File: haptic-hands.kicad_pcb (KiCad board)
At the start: 2 copper layers, 28.6 x 89 mm, 17 parts, among them M1 Motor_DC, SW1 SW_Push_45deg

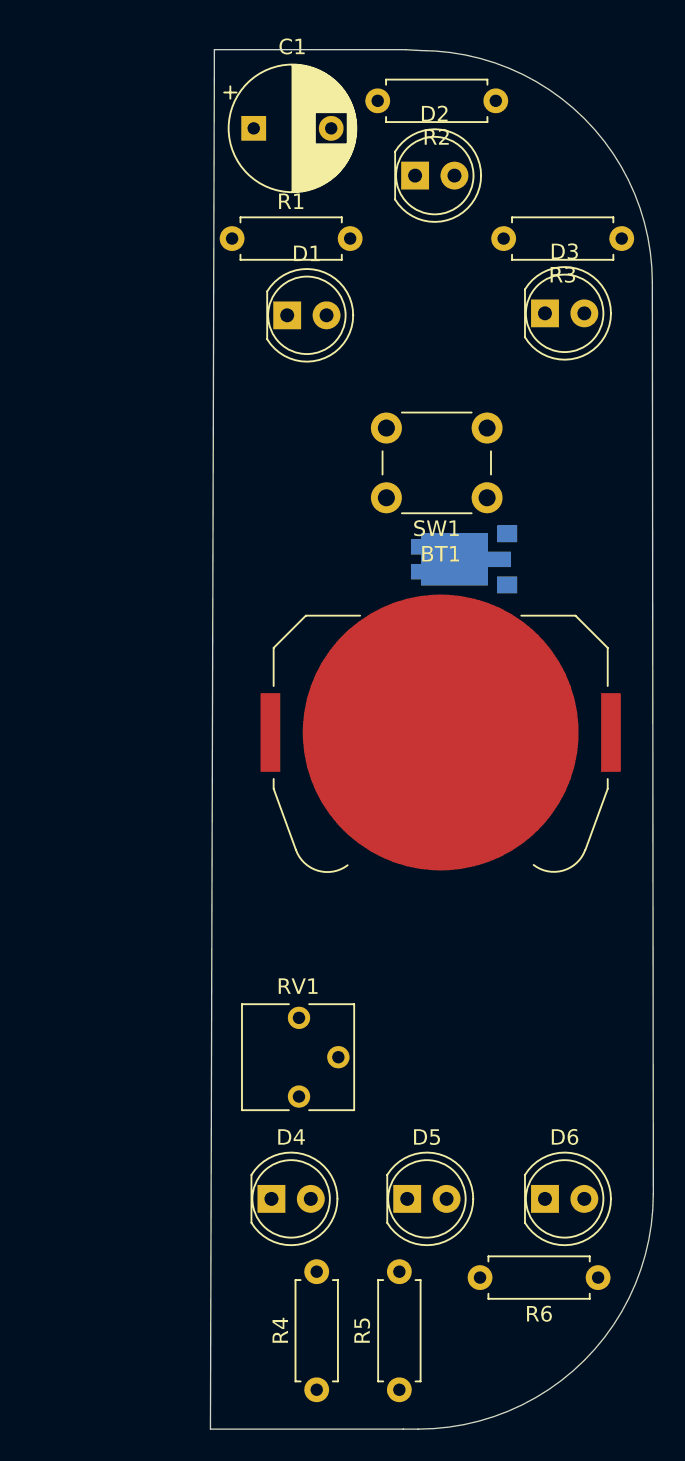
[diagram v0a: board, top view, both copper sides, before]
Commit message: Rearrange components, create board outline, route
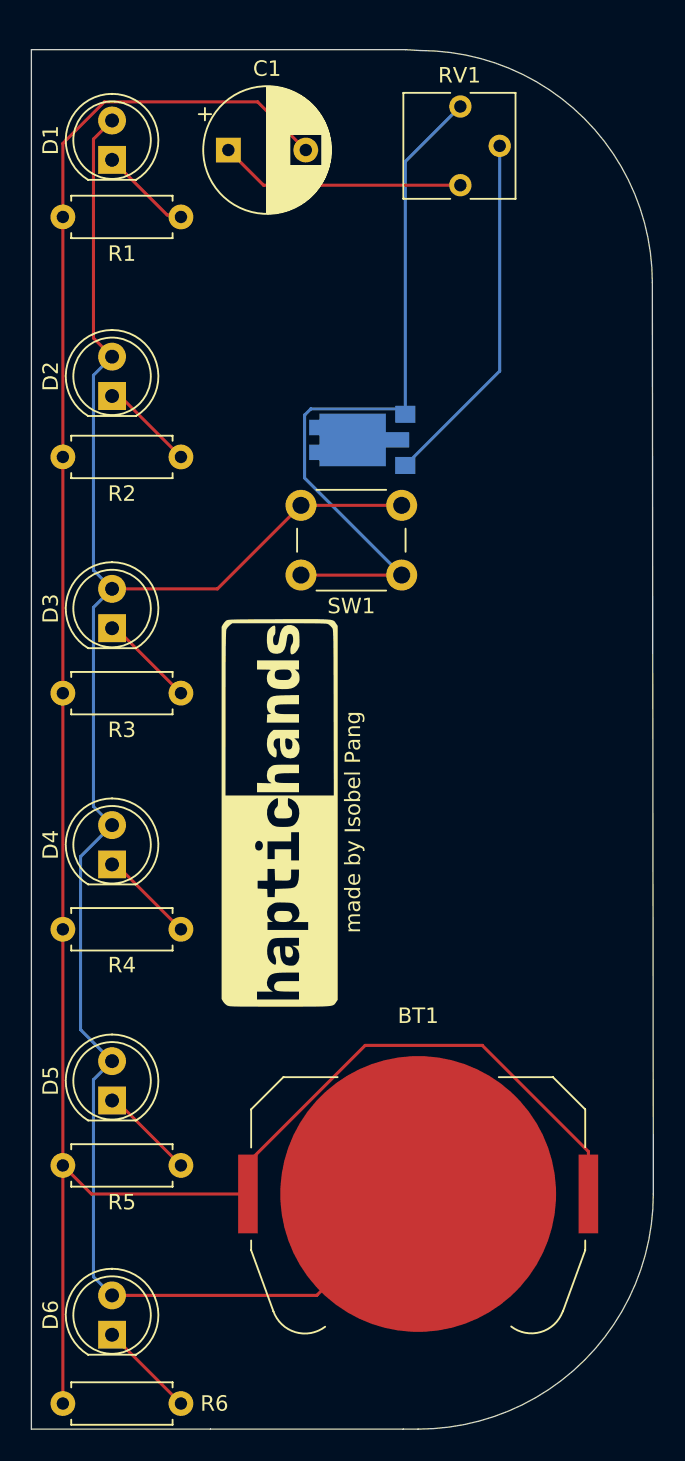
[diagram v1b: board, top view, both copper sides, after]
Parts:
- added G***: LOGO, LOGO, F.Cu at (129.5, 93.9)
- moved RV1 59.7 mm to (141.2, 53.3)
- moved R3 40.9 mm to (123.2, 86.1)
- moved D3 34.5 mm to (118.7, 81.9), turned to 90 degrees
- moved R4 31.0 mm to (123.2, 101.3), turned to 180 degrees
- moved R2 30.7 mm to (123.2, 70.9)
- moved BT1 29.8 mm to (138.5, 118.4)
- moved D6 29.3 mm to (118.7, 127.5), turned to 90 degrees
- moved R6 28.1 mm to (123.2, 132.0)
- moved D2 24.2 mm to (118.7, 66.9), turned to 90 degrees
- moved D4 23.9 mm to (118.7, 97.2), turned to 90 degrees
- moved R5 20.2 mm to (123.2, 116.6), turned to 180 degrees
- moved D5 20.1 mm to (118.7, 112.4), turned to 90 degrees
- moved D1 15.1 mm to (118.7, 51.7), turned to 90 degrees
- moved M1 10.1 mm to (133.3, 69.8)
- moved SW1 7.44 mm to (137.4, 78.5)
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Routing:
- net Net-(BT1-+): track 0.00 -> 144.8 mm
- net Net-(BT1--): track 0.00 -> 124.9 mm
- net Net-(M1--): track 0.00 -> 47.6 mm
- net Net-(M1-+): track 0.00 -> 23.2 mm
- net Net-(C1-Pad1): track 0.00 -> 15.9 mm
- net Net-(D6-K): track 0.00 -> 6.28 mm
- net Net-(D5-K): track 0.00 -> 6.18 mm
- net Net-(D3-K): track 0.00 -> 6.18 mm
- net Net-(D4-K): track 0.00 -> 6.18 mm
- net Net-(D2-K): track 0.00 -> 6.07 mm
- net Net-(D1-K): track 0.00 -> 5.97 mm
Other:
- board size 28.6 x 89 mm -> 40.1 x 89 mm
- board text added: "made by Isobel Pang"

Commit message: Route PCB
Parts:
- added G***: LOGO, LOGO, F.Cu at (138.4, 61.0)
- added G***: LOGO, LOGO, F.Cu at (137.4, 80.6)
- added G***: LOGO, LOGO, F.Cu at (146.8, 107.4)
- added G***: LOGO, LOGO, F.Cu at (148.0, 77.0)
- added G***: LOGO, LOGO, F.Cu at (119.5, 91.9)
- added G***: LOGO, LOGO, F.Cu at (137.5, 67.6)
- added G***: LOGO, LOGO, F.Cu at (138.2, 95.6)
- added G***: LOGO, LOGO, F.Cu at (125.6, 76.1)
- moved G*** 0.89 mm to (128.7, 93.9)

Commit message: Rework schematic
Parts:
- removed G*** (x9): LOGO, LOGO
- added SW2: SW_Push_45deg, Button_Switch_THT:SW_PUSH_6mm, F.Cu at (107.1, 73.6)
- added SW3: SW_Push_45deg, Button_Switch_THT:SW_PUSH_6mm, F.Cu at (107.1, 82.1)
- added SW4: SW_Push_45deg, Button_Switch_THT:SW_PUSH_6mm, F.Cu at (107.1, 90.7)
- added SW5: SW_Push_45deg, Button_Switch_THT:SW_PUSH_6mm, F.Cu at (107.1, 99.2)
- added SW6: SW_Push_45deg, Button_Switch_THT:SW_PUSH_6mm, F.Cu at (117.7, 65.0)
- added SW7: SW_Push_45deg, Button_Switch_THT:SW_PUSH_6mm, F.Cu at (117.7, 73.6)
- added SW8: SW_Push, Button_Switch_THT:SW_PUSH_6mm, F.Cu at (117.7, 82.1)
- M1: moved to F.Cu
- SW1: value SW_Push_45deg -> SW_Push
- moved RV1 52.5 mm to (149.0, 105.3)
- moved C1 47.6 mm to (147.1, 93.9)
- moved BT1 44.4 mm to (138.6, 74.0)
- moved SW1 33.2 mm to (107.1, 65.0), turned to 0 degrees
- moved R1 32.0 mm to (127.8, 87.1), turned to 0 degrees
- moved D6 30.0 mm to (100.1, 104.1), turned to 0 degrees
- moved M1 26.9 mm to (141.5, 95.4), turned to 0 degrees
- moved R6 25.1 mm to (127.8, 107.3), turned to 0 degrees
- moved D5 24.4 mm to (100.1, 96.6), turned to 0 degrees
- moved D1 24.0 mm to (100.1, 66.7), turned to 0 degrees
- moved R2 20.8 mm to (127.8, 91.1), turned to 0 degrees
- moved D4 20.3 mm to (100.1, 89.1), turned to 0 degrees
- moved D2 20.0 mm to (100.1, 74.2), turned to 0 degrees
- moved D3 18.7 mm to (100.1, 81.7), turned to 0 degrees
- moved R5 14.1 mm to (127.8, 103.3), turned to 0 degrees
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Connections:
- D1 pad 2: Net-(BT1--) -> Net-(D1-A)
- D2 pad 2: Net-(BT1--) -> Net-(D2-A)
- D3 pad 2: Net-(BT1--) -> Net-(D3-A)
- D4 pad 2: Net-(BT1--) -> Net-(D4-A)
- D5 pad 2: Net-(BT1--) -> Net-(D5-A)
- D6 pad 2: Net-(BT1--) -> Net-(D6-A)
- M1 pad 2: Net-(M1--) -> Net-(BT1--)
- RV1 pad 3: Net-(M1--) -> Net-(RV1-Pad3)
- SW1 pad 1: Net-(M1--) -> Net-(RV1-Pad3)
- SW1 pad 2: Net-(BT1--) -> Net-(SW1-Pad2)
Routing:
- net Net-(BT1-+): track 144.8 -> 0.00 mm
- net Net-(BT1--): track 124.9 -> 0.00 mm
- net Net-(M1--): track 47.6 -> 0.00 mm
- net Net-(M1-+): track 23.2 -> 0.00 mm
- net Net-(C1-Pad1): track 15.9 -> 0.00 mm
- net Net-(D6-K): track 6.28 -> 0.00 mm
- net Net-(D5-K): track 6.18 -> 0.00 mm
- net Net-(D3-K): track 6.18 -> 0.00 mm
- net Net-(D4-K): track 6.18 -> 0.00 mm
- net Net-(D2-K): track 6.07 -> 0.00 mm
- net Net-(D1-K): track 5.97 -> 0.00 mm
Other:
- board outline removed
- board text removed: "made by Isobel Pang"

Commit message: Rework PCB
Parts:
- BT1: moved to B.Cu
- M1: footprint Motors:Vybronics_VZ30C1T8219732L -> Connector_PinHeader_2.54mm:PinHeader_1x02_P2.54mm_Vertical; moved to B.Cu
- moved D6 69.3 mm to (165.3, 80.6)
- moved SW1 66.8 mm to (164.2, 99.6), turned to 90 degrees
- moved D5 60.9 mm to (158.8, 80.6)
- moved D4 53.0 mm to (152.4, 80.6)
- moved SW6 46.7 mm to (149.1, 99.6), turned to 90 degrees
- moved SW8 45.8 mm to (156.6, 106.1), turned to 90 degrees
- moved SW7 43.6 mm to (156.6, 93.1), turned to 90 degrees
- moved M1 26.2 mm to (166.5, 103.5), turned to 180 degrees
- moved SW2 26.0 mm to (108.0, 99.6), turned to 90 degrees
- moved SW3 25.3 mm to (115.5, 106.0), turned to 90 degrees
- moved RV1 23.0 mm to (166.6, 90.5)
- moved D3 21.6 mm to (121.6, 80.6)
- moved SW4 18.2 mm to (123.0, 99.5), turned to 90 degrees
- moved R6 17.1 mm to (144.9, 106.2)
- moved R5 17.1 mm to (144.9, 102.9)
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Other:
- board outline added: 66.2 x 37.9 mm

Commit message: Change layout (again)
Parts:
- moved D6 76.6 mm to (103.8, 126.2)
- moved SW6 76.6 mm to (87.6, 145.2)
- moved D1 76.6 mm to (47.2, 126.2)
- moved D2 76.6 mm to (53.7, 126.2)
- moved D3 76.6 mm to (60.1, 126.2)
- moved D4 76.6 mm to (90.9, 126.2)
- moved D5 76.6 mm to (97.3, 126.2)
- moved M1 76.6 mm to (105.0, 149.1)
- moved R1 76.6 mm to (63.6, 148.6)
- moved R2 76.6 mm to (63.6, 151.9)
- moved R3 76.6 mm to (73.5, 148.6)
- moved R4 76.6 mm to (73.5, 151.9)
- moved R5 76.6 mm to (83.4, 148.6)
- moved R6 76.6 mm to (83.4, 151.9)
- moved RV1 76.6 mm to (105.1, 136.1)
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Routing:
- net Net-(BT1--): track 0.00 -> 129.4 mm, vias 0 -> 2
- net Net-(BT1-+): track 0.00 -> 85.3 mm, vias 0 -> 2
- net Net-(D4-A): track 0.00 -> 54.8 mm
- net Net-(C1-Pad1): track 0.00 -> 38.2 mm, vias 0 -> 1
- net Net-(D4-K): track 0.00 -> 36.3 mm
- net Net-(D6-K): track 0.00 -> 34.1 mm
- net Net-(D2-A): track 0.00 -> 33.9 mm
- net Net-(D1-K): track 0.00 -> 31.8 mm
- net Net-(D3-K): track 0.00 -> 31.3 mm
- net Net-(D2-K): track 0.00 -> 30.7 mm
- net Net-(D5-K): track 0.00 -> 28.1 mm
- net Net-(SW1-Pad2): track 0.00 -> 26.2 mm, vias 0 -> 1
- net Net-(D5-A): track 0.00 -> 22.6 mm
- net Net-(D3-A): track 0.00 -> 20.3 mm
- net Net-(D1-A): track 0.00 -> 19.5 mm
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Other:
- board size 66.2 x 37.9 mm -> 67 x 38 mm
